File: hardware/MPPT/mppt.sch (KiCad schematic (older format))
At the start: 22 parts

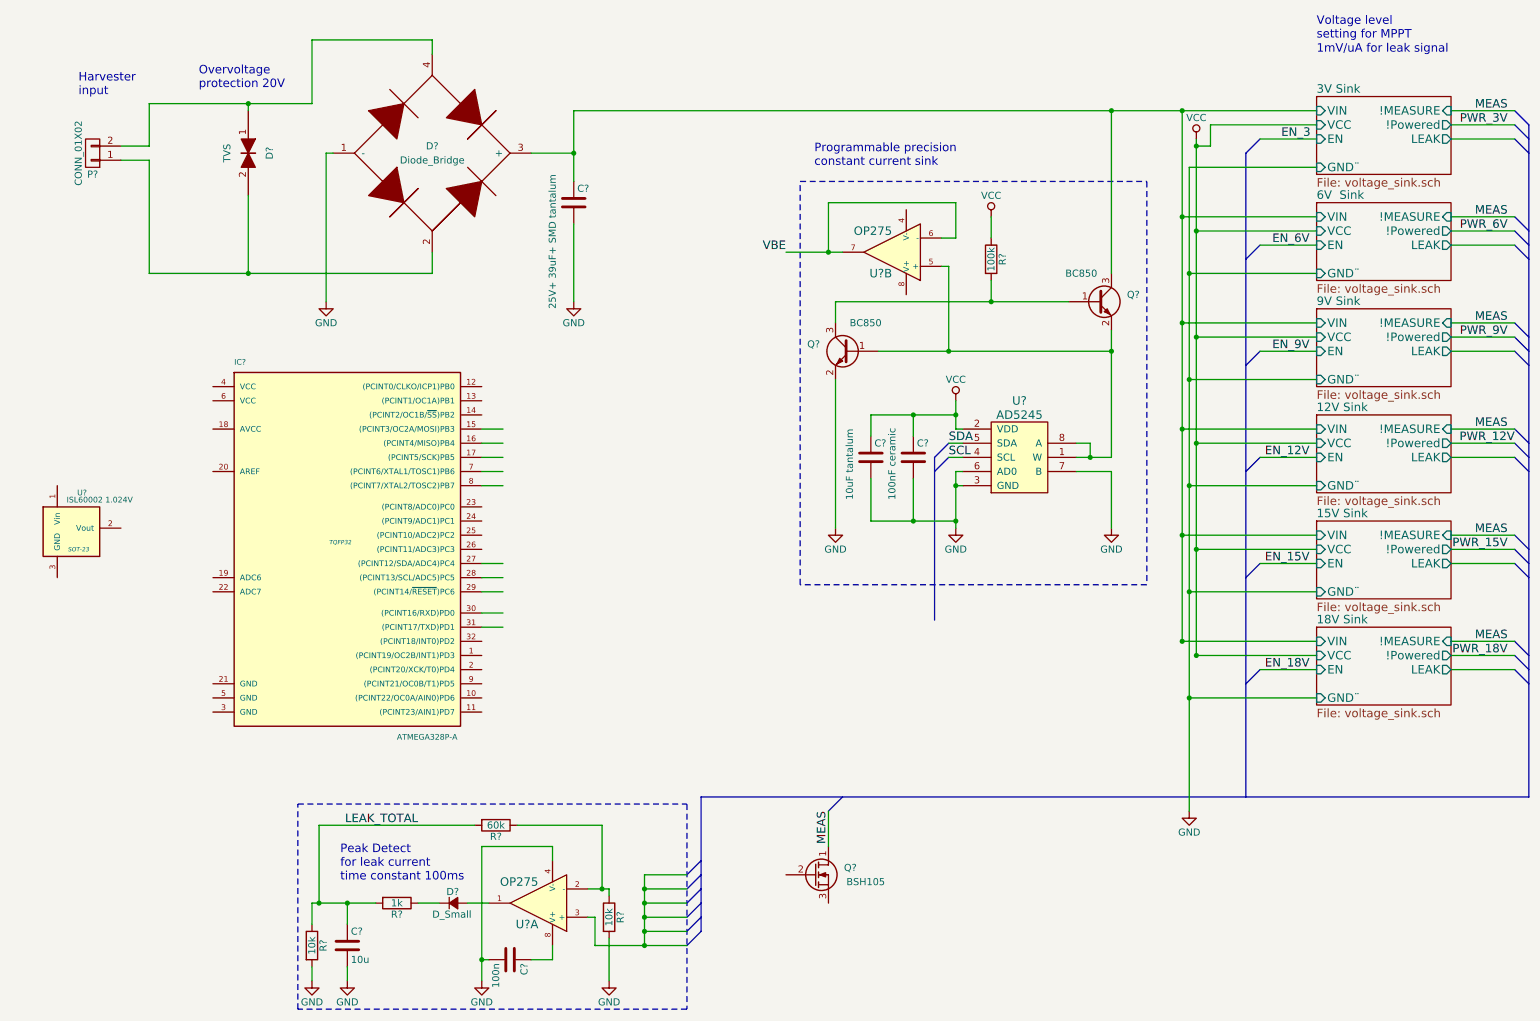
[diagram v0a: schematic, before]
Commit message: Add signaling LEDs to voltage clamps, adjust time constant on peak detect.
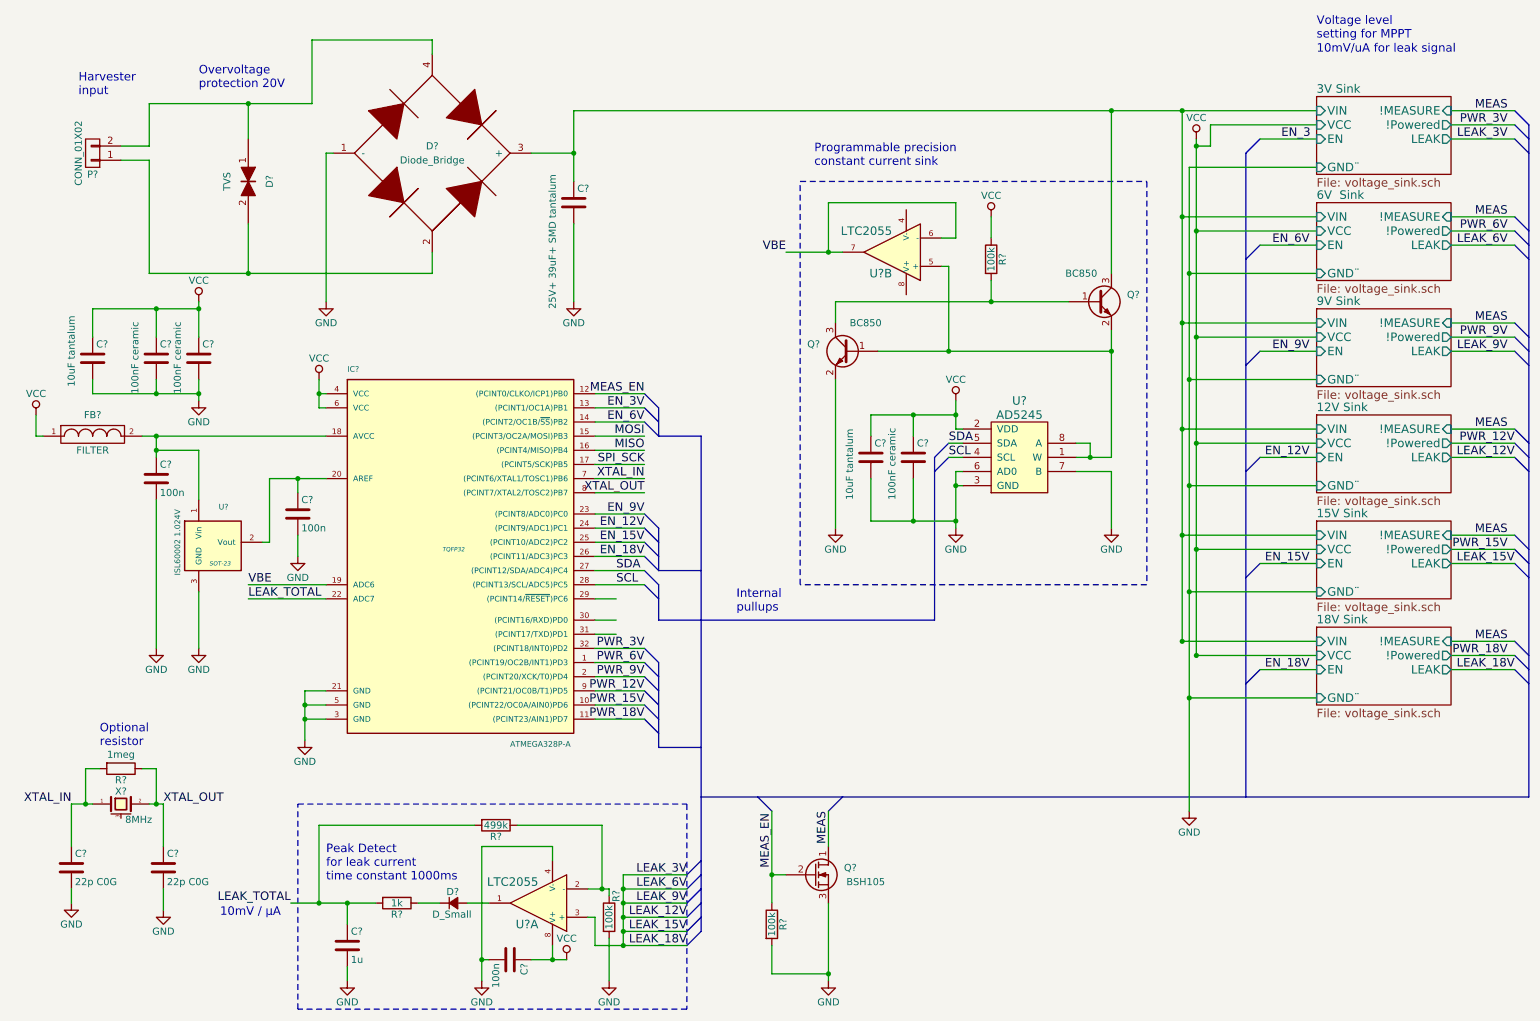
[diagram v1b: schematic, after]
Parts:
- removed R?: 10k, symbol R
- added C? (x2): 22p C0G, symbol C
- added C? (x2): 100n, symbol C
- added C? (x2): 100nF ceramic, symbol C
- added C?: 10uF tantalum, symbol C
- added FB?: FILTER, symbol FILTER
- added R?: 1meg, symbol R
- added R?: 100k, symbol R
- added X?: 8MHz, symbol CRYSTAL_SMD
- C?: value 10u -> 1u
- R?: value 60k -> 499k
- R?: value 10k -> 100k
- U? (x2): value OP275 -> LTC2055
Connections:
- net labels added: EN_3V, LEAK_12V, LEAK_15V, LEAK_18V, LEAK_3V, LEAK_6V, LEAK_9V, MEAS_EN, MISO, MOSI, SPI_SCK, XTAL_IN, XTAL_OUT
- wire segments 137 -> 193
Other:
- note added: "10mV / µA"
- note added: "10mV/uA for leak signal"
- note added: "Internal \npullups"
- note added: "Optional \nresistor"
- note added: "Peak Detect\nfor leak current\ntime constant 1000ms"
- note removed: "1mV/uA for leak signal"
- note removed: "Peak Detect\nfor leak current\ntime constant 100ms"
- moved on the sheet: D?, IC?, U?

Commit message: Reduce complexity of MPPT schematic
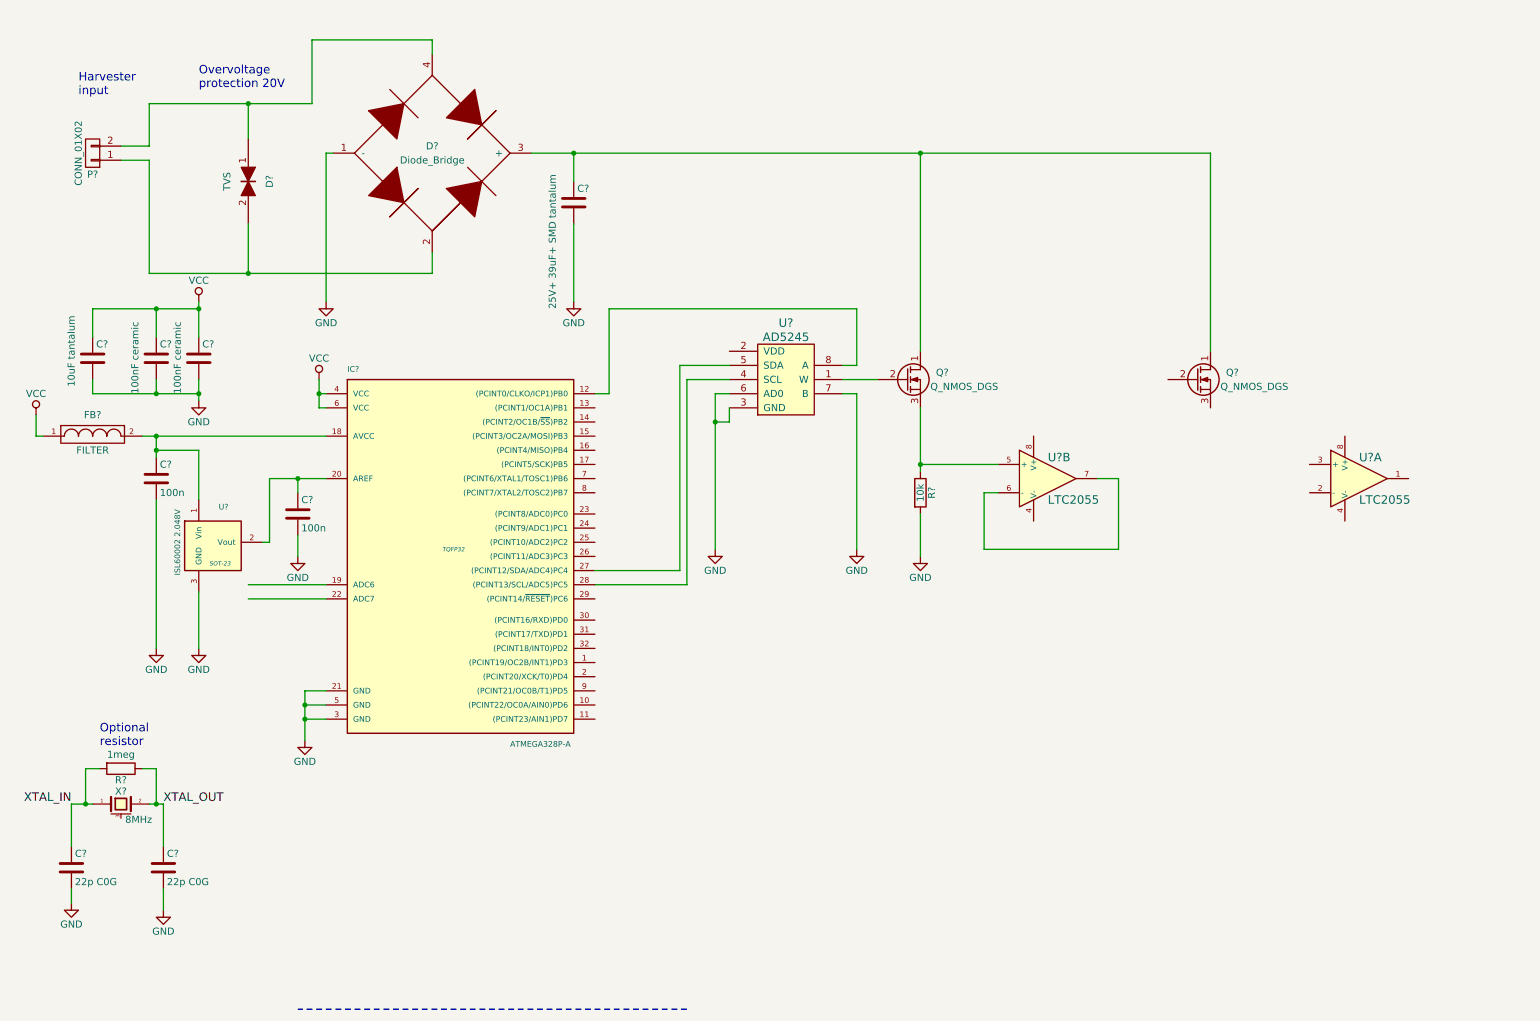
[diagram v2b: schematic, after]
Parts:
- removed C?: 100nF ceramic, symbol C
- removed C?: 10uF tantalum, symbol C
- removed C?: 1u, symbol C
- removed C?: 100n, symbol C
- removed D?: D_Small, symbol D_Small
- removed Q? (x2): BC850, symbol Q_NPN_BEC
- removed Q?: BSH105, symbol Q_NMOS_DGS
- removed R? (x3): 100k, symbol R
- removed R?: 499k, symbol R
- removed R?: 1k, symbol R
- removed U?: AD5245, symbol AD5245
- removed U? (x2): LTC2055, symbol OP275
- added Q? (x2): Q_NMOS_DGS, symbol Q_NMOS_DGS
- added R?: 10k, symbol R
- added U? (x2): LTC2055, symbol OP275
- added U?: AD5245, symbol AD5245
- U?: value ISL60002 1.024V -> ISL60002 2.048V
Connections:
- net labels removed: EN_12V, EN_15V, EN_18V, EN_3, EN_3V, EN_6V, EN_9V, LEAK_12V, LEAK_15V, LEAK_18V, LEAK_3V, LEAK_6V, LEAK_9V, LEAK_TOTAL, MEAS, MEAS_EN, MISO, MOSI, PWR_12V, PWR_15V, PWR_18V, PWR_3V, PWR_6V, PWR_9V, SCL, SDA, SPI_SCK, VBE
- wire segments 193 -> 85
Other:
- note removed: "10mV / µA"
- note removed: "10mV/uA for leak signal"
- note removed: "Internal \npullups"
- note removed: "Peak Detect\nfor leak current\ntime constant 1000ms"
- note removed: "Programmable precision \nconstant current sink"
- note removed: "Voltage level \nsetting for MPPT"
